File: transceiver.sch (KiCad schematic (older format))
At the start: 0 parts

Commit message: Added CC1190 library
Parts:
- added U3: CC1200, Package_DFN_QFN:QFN-32-1EP_5x5mm_P0.5mm_EP3.45x3.45mm, symbol RF:CC1200
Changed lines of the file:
@@
 $Descr A4 11693 8268
 encoding utf-8
-Sheet 6 6
+Sheet 4 6
 Title ""
 Date ""
@@
 Comment4 ""
 $EndDescr
+$Comp
+L RF:CC1200 U3
+U 1 1 601884DE
+P 6000 4000
+F 0 "U3" H 6000 5267 50  0000 C CNN
+F 1 "CC1200" H 6000 5176 50  0000 C CNN
+F 2 "Package_DFN_QFN:QFN-32-1EP_5x5mm_P0.5mm_EP3.45x3.45mm" H 6600 5150 50  0001 C CNN
+F 3 "http://www.ti.com/lit/ds/symlink/cc1200.pdf" H 5500 5150 50  0001 C CNN
+	1    6000 4000
+	1    0    0    -1
+$EndComp
 $EndSCHEMATC

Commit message: Started work on CC1200
might not be actual final tranciever
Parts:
- added C18, C19, C20, C21, C22, C23, C24, C25, C26, C27, C28, C29, C30, C31, C32: C, symbol Device:C
- added R6: R, symbol Device:R
- added Y1: Crystal_GND23, symbol Device:Crystal_GND23
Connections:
- net ~CS: now reaches U3.11 (~CS~)
- net +3.3VA: now reaches U3.13 (AVDD_IF)
- net +3.3VA: now also U3.15 (AVDD_RF), U3.22 (AVDD_SYNTH1), U3.25 (AVDD_PFD_CHP), U3.27 (AVDD_SYNTH2), U3.28 (AVDD_XOSC), C20.1, C21.1, C22.1, C24.1, C26.1, C28.1, C30.1, C31.1, C32.1
- net at U3.14 (RBIAS): now also R6.2
- net at U3.21 (DCPL_VCO): now also C27.1
- net at U3.23 (LPF0): now also C19.1
- net at U3.24 (LPF1): now also C19.2
- net at U3.26 (DCPL_PFD_CHP): now also C25.1
- net at U3.29 (DCPL_XOSC): now also C23.1
- net at U3.30 (XOSC_Q1): now also Y1.1
- net at U3.31 (XOSC_Q2): now also Y1.4
- net GND: now reaches U3.33 (GND_EP)
- net GND: now also C18.2, C20.2, C21.2, C22.2, C23.2, C24.2, C25.2, C26.2, C27.2, C28.2, C29.2, C30.2, C31.2, C32.2, R6.1
- net at U3.6 (DCPL): now also C29.1
- net SI: now reaches U3.7 (SI)
- net SCLK: now reaches U3.8 (SCLK)
- net SO: now reaches U3.9 (SO(GPIO1))
- new net: C18.1, Y1.2, Y1.3
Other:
- note added: "Connecto to solid \nground plane\n"
- moved on the sheet: U3

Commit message: Started work on MCU
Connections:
- net ~RESET: now reaches U3.2 (~RESET~)
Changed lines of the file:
@@
 Wire Wire Line
 	8300 2200 8650 2200
+Text HLabel 5300 1800 0    59   Input ~ 0
+~RESET
+Wire Wire Line
+	5300 1800 5550 1800
 $EndSCHEMATC

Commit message: More work on tranciever and PA
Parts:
- added C57, C58, C59, C60, C61, C62, C63, C64, C65, C66, C67, C68, C69, C71, C72, C73, C74, C75, C76: C, symbol Device:C
- added FB2: Ferrite_Bead, symbol Device:Ferrite_Bead
- added L10, L11, L12, L13, L14, L15, L16, L17: L, symbol Device:L
- added R13: R, symbol Device:R
- added TP2: VDD_CC1200, symbol Connector:TestPoint
- Y1: value Crystal_GND23 -> 40 Mhz crystal
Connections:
- net +3.3VA is gone; now on net VDD_CC1200: C20.1, C21.1, C22.1, C24.1, C26.1, C28.1, C30.1, C31.1, C32.1, U3.13 (AVDD_IF), U3.15 (AVDD_RF), U3.22 (AVDD_SYNTH1), U3.25 (AVDD_PFD_CHP), U3.27 (AVDD_SYNTH2), U3.28 (AVDD_XOSC)
- net GND: now also U3.32 (EXT_XOSC), C57.2, C58.2, C59.2, C60.2, C61.2, C62.2, C63.2, C64.2, C65.2, C66.2, C68.2, C74.2, C76.1, L12.2
- net VDD_CC1200: now reaches U3.1 (VDD_GUARD)
- net VDD_CC1200: now also U3.12 (DVDD), U3.5 (DVDD), C61.1, C62.1, C63.1, C64.1, C65.1, C66.1, C67.2, C68.1, FB2.1, R13.2, TP2.1
- net GPIO0: now reaches U3.10 (GPIO0)
- net at U3.17 (PA): now also C69.2, L10.1
- net at U3.18 (TRX_SW): now also C72.1, L16.2
- net at U3.19 (LNA_P): now also C73.2, L11.1, L12.1
- net at U3.20 (LNA_N): now also C76.2, L11.2, L15.1
- net GPIO3: now reaches U3.3 (GPIO3)
- net at U3.30 (XOSC_Q1), Y1.1: now also C58.1, C59.1
- net at U3.31 (XOSC_Q2), Y1.4: now also C57.1
- net GPIO2: now reaches U3.4 (GPIO2)
- new net: C67.1, L10.2, R13.1
- new net: C69.1, C71.2, L13.1
- new net: C71.1, C72.2, L13.2, L14.1
- new net: C74.1, C75.2, L14.2, L17.1
- new net: C73.1, L15.2, L16.1
- new net +3V3: C60.1, FB2.2
- new net CC1200_RFIO: C75.1, L17.2
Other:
- note added: "Can be replaced by \nhttps://www.johansontechnology.com/\ndatasheets/0900PC15J0013/0900PC15J0013.pdf"
- moved on the sheet: C18, C19, C20, C21, C22, C23, C24, C25, C26, C27, C28, C29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

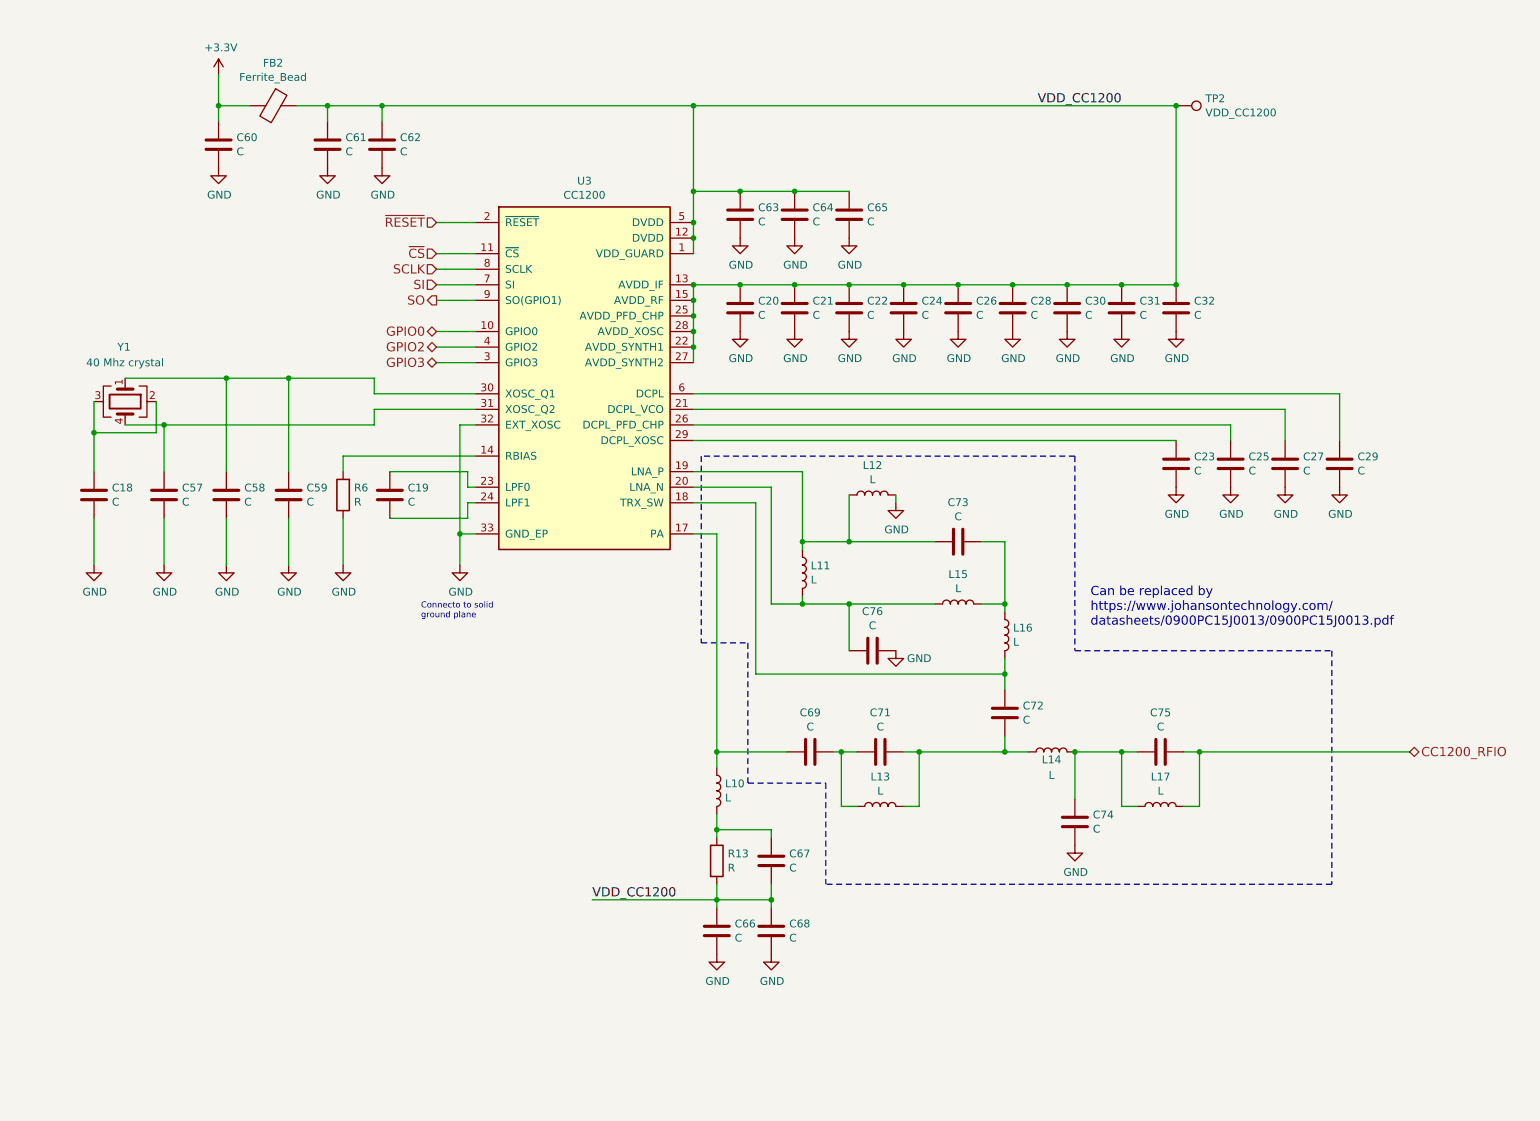
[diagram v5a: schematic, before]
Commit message: Added mount for RFM98/95
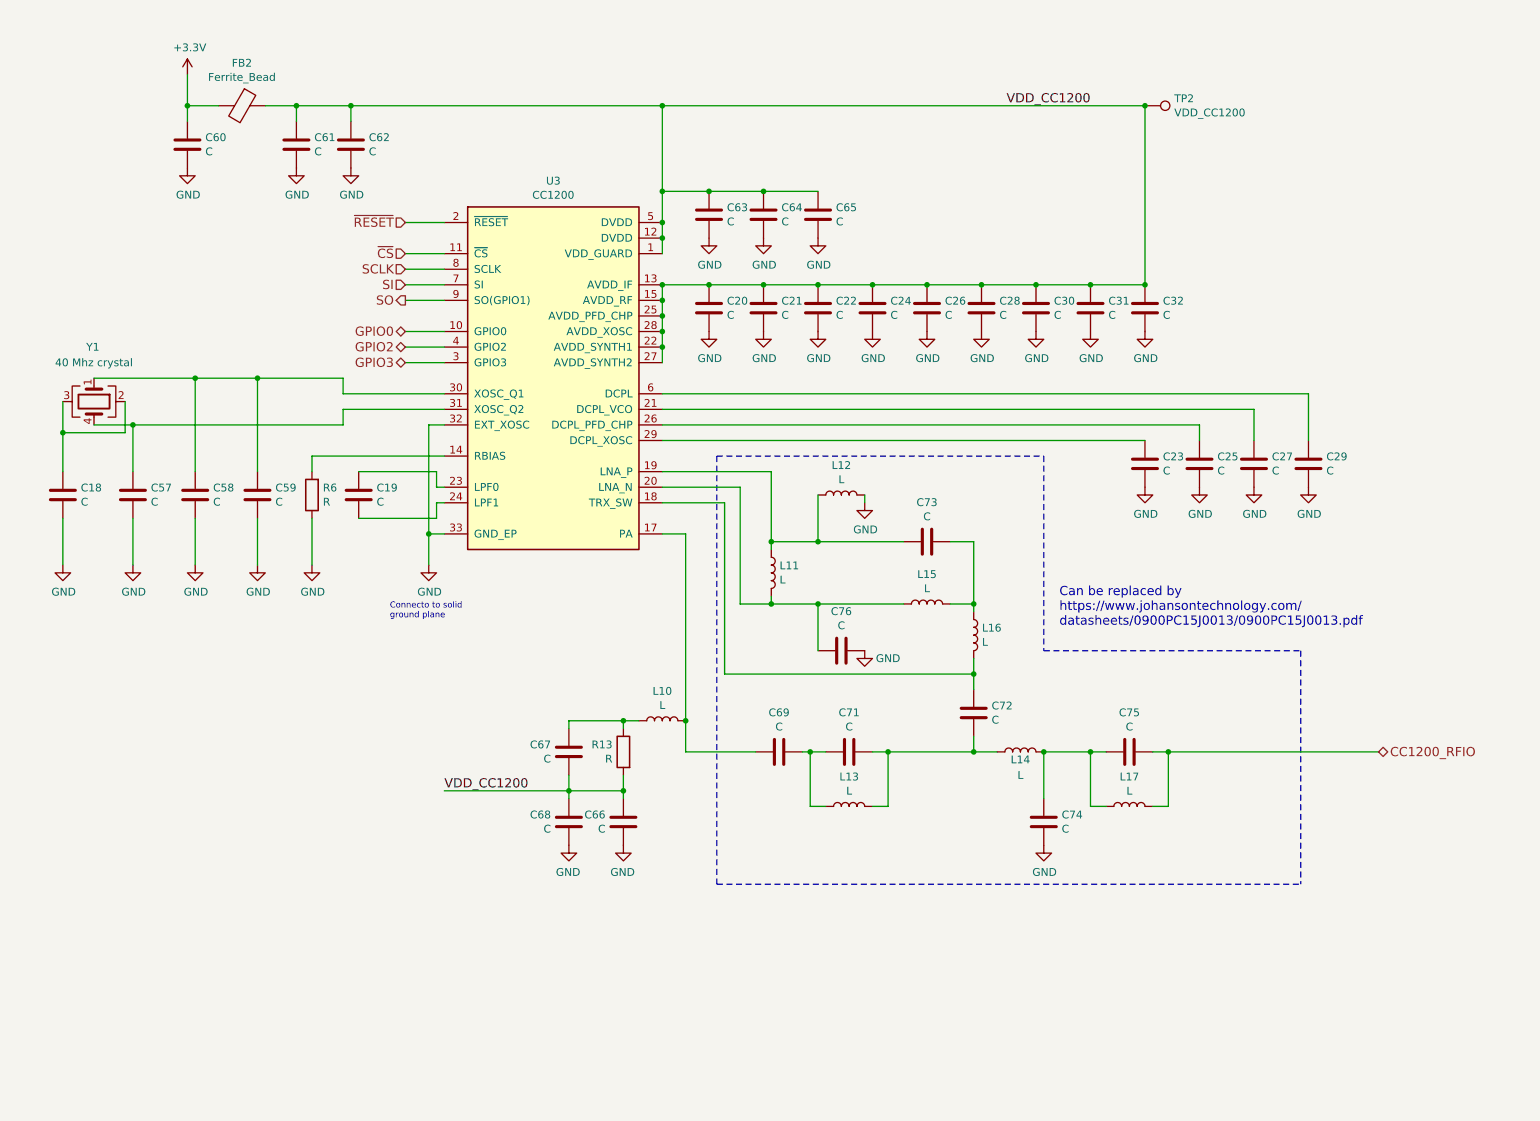
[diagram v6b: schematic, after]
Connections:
- net at C69.2, U3.17 (PA): now also L10.2; no longer L10.1
- net at C67.1, R13.1: now also L10.1; no longer L10.2
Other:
- moved on the sheet: C18, C19, C20, C21, C22, C23, C24, C25, C26, C27, C28, C29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

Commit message: Added component values for tranciever and PA
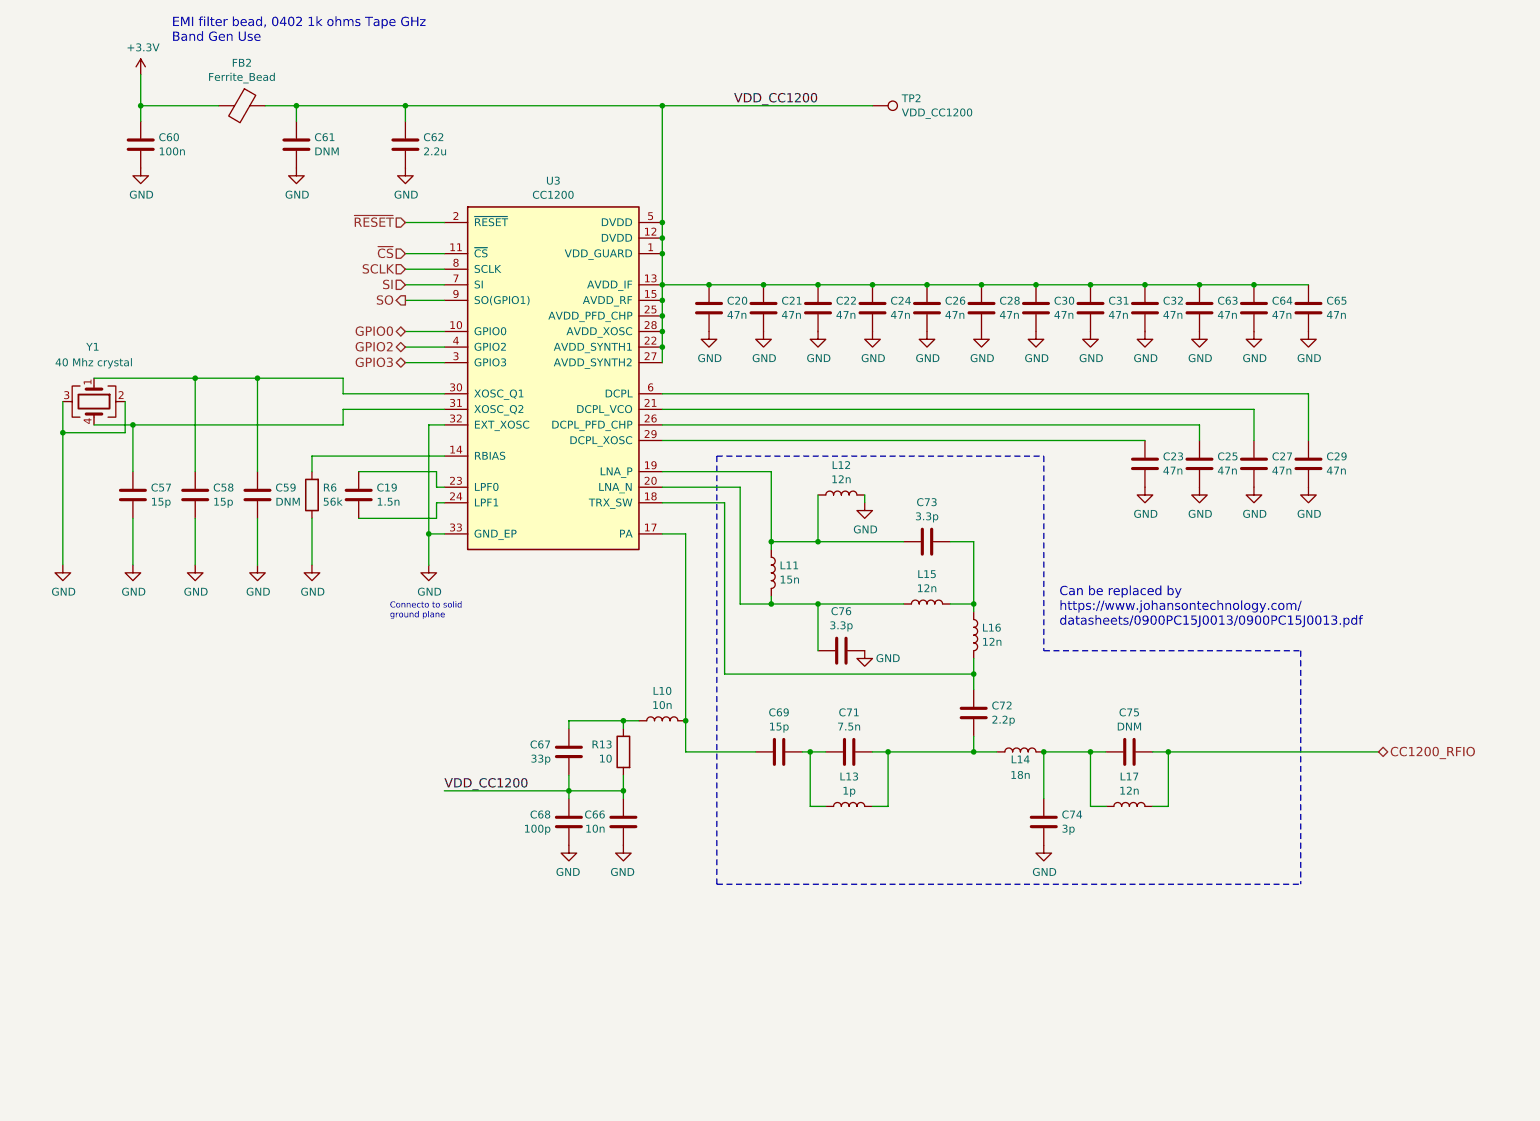
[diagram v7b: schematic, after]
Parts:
- removed C18: C, symbol Device:C
- C19: value C -> 1.5n
- C20, C21, C22, C23, C24, C25, C26, C27, C28, C29, C30, C31, C32, C63, C64, C65: value C -> 47n
- C57, C58, C69: value C -> 15p
- C59, C61, C75: value C -> DNM
- C60: value C -> 100n
- C62: value C -> 2.2u
- C66: value C -> 10n
- C67: value C -> 33p
- C68: value C -> 100p
- C71: value C -> 7.5n
- C72: value C -> 2.2p
- C73, C76: value C -> 3.3p
- C74: value C -> 3p
- L10: value L -> 10n
- L11: value L -> 15n
- L12, L15, L16, L17: value L -> 12n
- L13: value L -> 1p
- L14: value L -> 18n
- R13: value R -> 10
- R6: value R -> 56k
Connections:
- net GND: now also Y1.2, Y1.3
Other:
- note added: "EMI filter bead, 0402 1k ohms Tape GHz\nBand Gen Use"
- moved on the sheet: C60, C62, TP2

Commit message: Small changes to schematic
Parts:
- removed C63, C64, C65: 47n, symbol Device:C
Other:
- note added: "Can also use temperature compensated crystal.\nBut probably not neccecairy."
- note added: "Reference design by TI:\nhttps://www.ti.com/tool/CC1120-CC1190EM868RD\n"
- note removed: "EMI filter bead, 0402 1k ohms Tape GHz\nBand Gen Use"
- moved on the sheet: C19, C20, C21, C22, C23, C24, C25, C26, C27, C28, C29, C30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
